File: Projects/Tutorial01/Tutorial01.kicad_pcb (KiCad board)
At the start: 2 copper layers, 3 parts

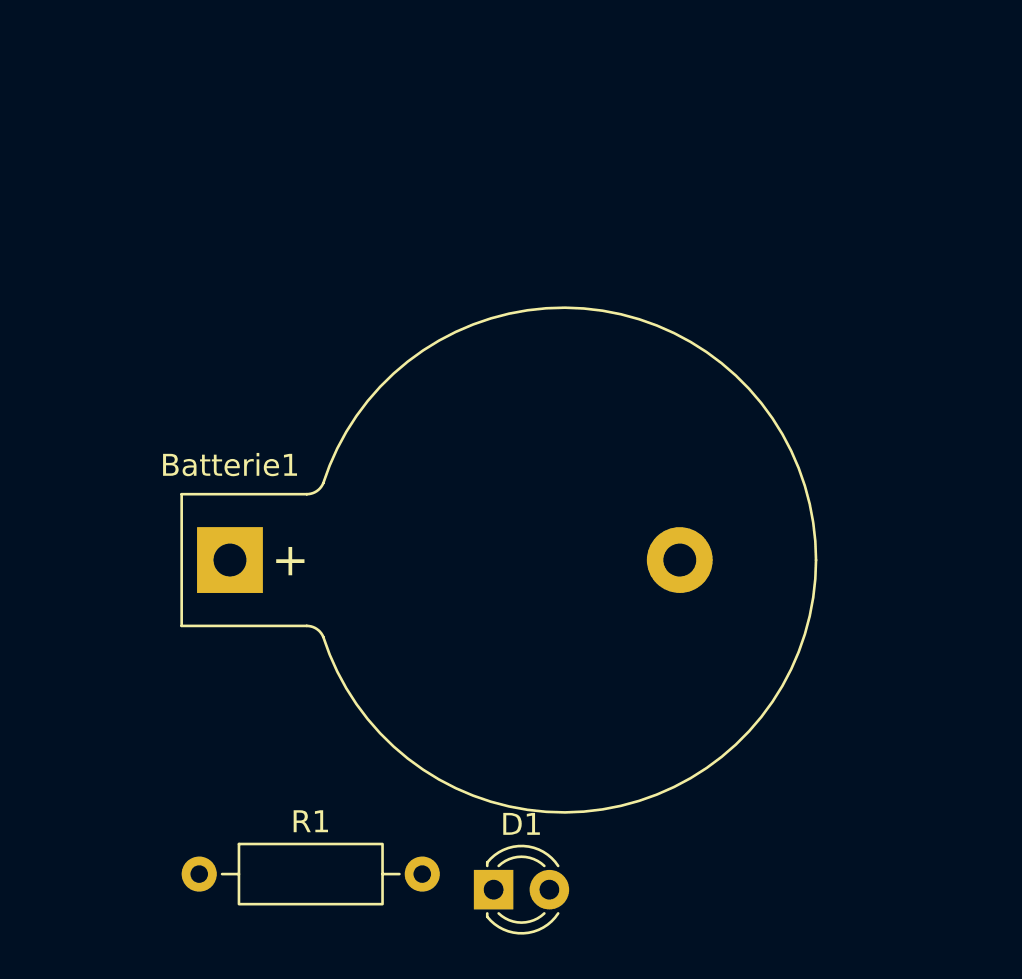
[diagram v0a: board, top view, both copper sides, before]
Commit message: 20251114 Schaltplan mit Batterie 9V, eine rote Diode 3 mm Durchmnesser und ein Widerstand 220 ohm
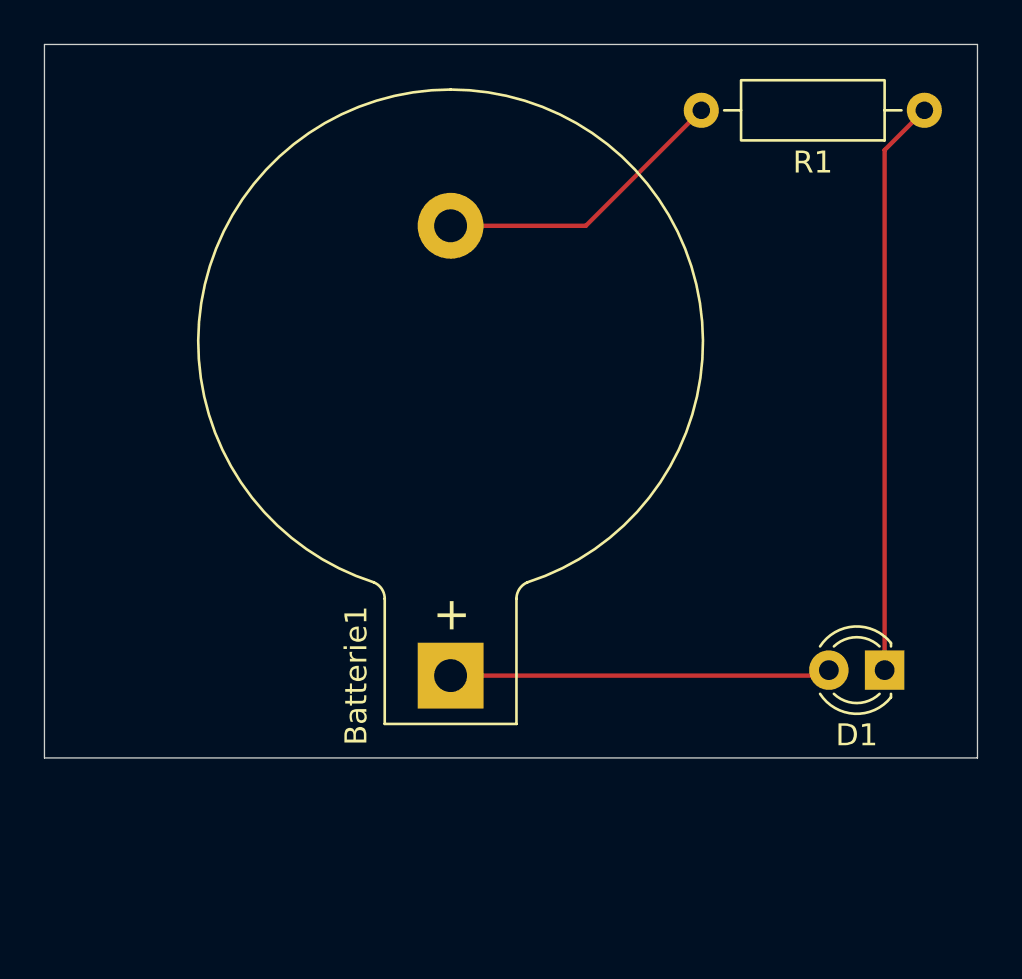
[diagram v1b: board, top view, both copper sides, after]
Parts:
- moved R1 48.0 mm to (145.1, 88.0), turned to 180 degrees
- moved D1 20.4 mm to (143.3, 113.5), turned to 180 degrees
- moved Batterie1 11.3 mm to (123.5, 113.8), turned to 90 degrees
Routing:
- net Net-(D1-K): track 0.00 -> 26.2 mm
- net Net-(Batterie1-+): track 0.00 -> 17.3 mm
- net Net-(Batterie1--): track 0.00 -> 13.6 mm
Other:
- board outline added: 42.5 x 32.5 mm
